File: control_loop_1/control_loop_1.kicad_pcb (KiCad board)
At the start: 2 copper layers, 100 x 95 mm, 148 parts, among them J1 I_MEAS, J10 GND, J11 -5V, J12 POW_OUT, J13 I_SET, J14 U_SET, J15 GND, J16 CTR_MODE, J17 GND, J18 CTR_MODE, J19 Limit_conn, J2 U_MEAS, J20 Trig_conn, J21 CTR_SIG, J22 CTR_SIG_OUT, J23 GND, J24 Conn_01x04, J3 GND, J4 GND, J5 +15V, J6 GND, J7 -15V, J8 SET_CONN, J9 +5V, Q1 2N7002BK, Q2 2N7002BK, Q3 2N7002BK, Q4 2N7002BK, U1 LM317EMPX/NOPB, U2 LM337IMP/NOPB, U4 OPA1679IDR, U5 OPA1679IDR, U6 DG469EQ-T1-E3, U7 OPA1679IDR, U8 LM393BIDR, U9 LM393BIDR

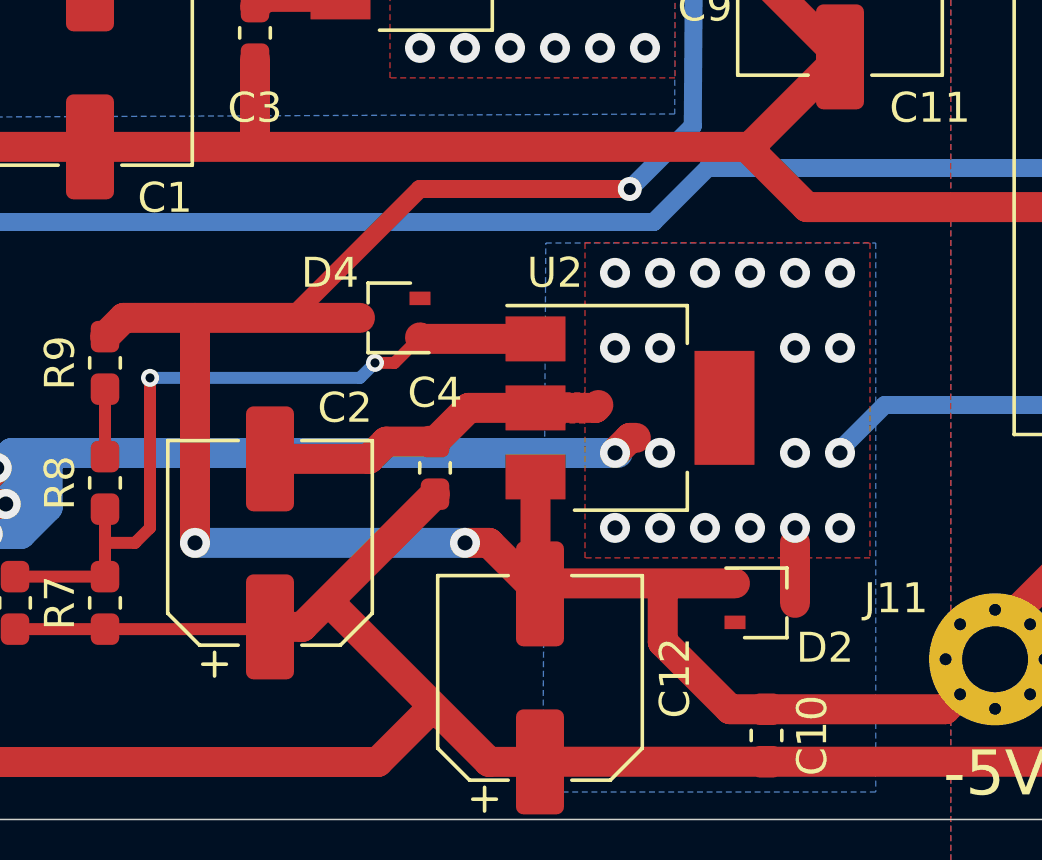
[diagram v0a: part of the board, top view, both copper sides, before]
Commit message: fixed diodes orientation
negative volt regulator - reversed diodes fixed
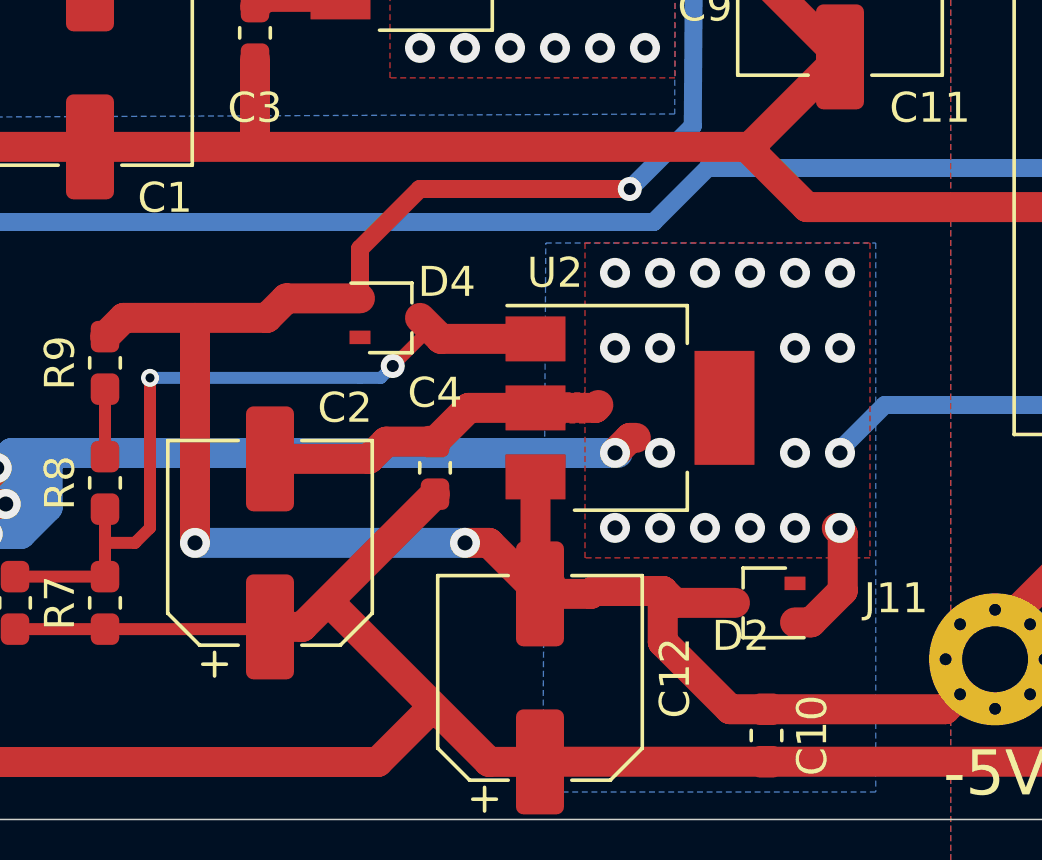
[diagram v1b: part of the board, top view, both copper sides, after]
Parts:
- turned D2 to 180 degrees
- turned D4 to 0 degrees
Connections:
- D2 pad 1: -5V -> -15V
- D2 pad 3: -15V -> -5V
- D4 pad 1: Net-(C7-Pad2) -> -5V
- D4 pad 3: -5V -> Net-(C7-Pad2)
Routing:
- net -15V: track 93.9 -> 96.1 mm
- net -5V: track 279.0 -> 278.2 mm
- net Net-(C7-Pad2): track 25.4 -> 26.2 mm
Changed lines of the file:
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@@
     (thickness 1.6)
     (drawings 70)
-    (tracks 1134)
+    (tracks 1144)
     (zones 0)
     (modules 148)
@@
   )
   (setup
-    (last_trace_width 0.25)
+    (last_trace_width 1)
     (user_trace_width 0.3)
     (user_trace_width 0.4)
@@
   )
   (module Package_TO_SOT_SMD:SOT-323_SC-70 (layer F.Cu)
-    (at 121.308 126.796 180)
+    (at 121.308 126.796)
     (descr "SOT-323, SC-70")
     (tags "SOT-323 SC-70")
     (attr smd)
-    (fp_text reference D4 (at 2 1.5) (layer F.SilkS)
+    (fp_text reference D4 (at 1.892 -1.196) (layer F.SilkS)
       (effects (font (size 1 1) (thickness 0.15)))
     )
@@
       (effects (font (size 0.5 0.5) (thickness 0.075)))
     )
-    (pad 3 smd rect (at 1 0 90) (size 0.45 0.7) (layers F.Cu F.Paste F.Mask)
-      (net 7 -5V))
-    (pad 2 smd rect (at -1 0.65 90) (size 0.45 0.7) (layers F.Cu F.Paste F.Mask)
-      (net 33 "Net-(D4-Pad2)"))
-    (pad 1 smd rect (at -1 -0.65 90) (size 0.45 0.7) (layers F.Cu F.Paste F.Mask)
+    (pad 3 smd rect (at 1 0 270) (size 0.45 0.7) (layers F.Cu F.Paste F.Mask)
       (net 5 "Net-(C7-Pad2)"))
+    (pad 2 smd rect (at -1 0.65 270) (size 0.45 0.7) (layers F.Cu F.Paste F.Mask)
+      (net 33 "Net-(D4-Pad2)"))
+    (pad 1 smd rect (at -1 -0.65 270) (size 0.45 0.7) (layers F.Cu F.Paste F.Mask)
+      (net 7 -5V))
     (model ${KISYS3DMOD}/Package_TO_SOT_SMD.3dshapes/SOT-323_SC-70.wrl
       (at (xyz 0 0 0))
@@
   )
   (module Package_TO_SOT_SMD:SOT-323_SC-70 (layer F.Cu)
-    (at 133.808 136.296)
+    (at 133.808 136.296 180)
     (descr "SOT-323, SC-70")
     (tags "SOT-323 SC-70")
     (attr smd)
-    (fp_text reference D2 (at 2 1.5) (layer F.SilkS)
+    (fp_text reference D2 (at 0.808 -1.104) (layer F.SilkS)
       (effects (font (size 1 1) (thickness 0.15)))
     )
@@
       (effects (font (size 0.5 0.5) (thickness 0.075)))
     )
-    (pad 3 smd rect (at 1 0 270) (size 0.45 0.7) (layers F.Cu F.Paste F.Mask)
-      (net 3 -15V))
-    (pad 2 smd rect (at -1 0.65 270) (size 0.45 0.7) (layers F.Cu F.Paste F.Mask)
-      (net 31 "Net-(D2-Pad2)"))
-    (pad 1 smd rect (at -1 -0.65 270) (size 0.45 0.7) (layers F.Cu F.Paste F.Mask)
+    (pad 3 smd rect (at 1 0 90) (size 0.45 0.7) (layers F.Cu F.Paste F.Mask)
       (net 7 -5V))
+    (pad 2 smd rect (at -1 0.65 90) (size 0.45 0.7) (layers F.Cu F.Paste F.Mask)
+      (net 31 "Net-(D2-Pad2)"))
+    (pad 1 smd rect (at -1 -0.65 90) (size 0.45 0.7) (layers F.Cu F.Paste F.Mask)
+      (net 3 -15V))
     (model ${KISYS3DMOD}/Package_TO_SOT_SMD.3dshapes/SOT-323_SC-70.wrl
       (at (xyz 0 0 0))
@@
   (segment (start 123.933 129.796) (end 126.158 129.796) (width 1) (layer F.Cu) (net 3))
   (segment (start 122.808 130.921) (end 123.933 129.796) (width 1) (layer F.Cu) (net 3))
-  (segment (start 134.808 136.296) (end 134.808 135.071) (width 1) (layer F.Cu) (net 3))
-  (segment (start 134.808 135.071) (end 134.808 134.296) (width 1) (layer F.Cu) (net 3))
   (segment (start 129.307999 130.796001) (end 129.503999 130.796001) (width 1) (layer F.Cu) (net 3))
   (segment (start 128.808 131.296) (end 129.307999 130.796001) (width 1) (layer F.Cu) (net 3))
@@
   (segment (start 159.836 129.7) (end 137.8 129.7) (width 0.6) (layer B.Cu) (net 3))
   (segment (start 137.8 129.7) (end 136.3 131.2) (width 0.6) (layer B.Cu) (net 3))
+  (segment (start 135.343002 136.946) (end 136.4 135.889002) (width 1) (layer F.Cu) (net 3))
+  (segment (start 134.808 136.946) (end 135.343002 136.946) (width 1) (layer F.Cu) (net 3))
+  (segment (start 136.4 135.889002) (end 136.4 134) (width 1) (layer F.Cu) (net 3))
+  (segment (start 136.4 134) (end 136.2 133.8) (width 1) (layer F.Cu) (net 3))
   (segment (start 130.458 107.646) (end 130.108 107.296) (width 1) (layer F.Cu) (net 4))
   (segment (start 131.808 107.646) (end 130.458 107.646) (width 1) (layer F.Cu) (net 4))
@@
   (segment (start 119.308 108.796) (end 119.808 108.796) (width 0.4) (layer F.Cu) (net 4))
   (segment (start 116.683 102.796) (end 116.683 105.796) (width 0.4) (layer F.Cu) (net 4))
-  (segment (start 122.358 127.496) (end 122.308 127.446) (width 1) (layer F.Cu) (net 5))
-  (segment (start 126.158 127.496) (end 122.358 127.496) (width 1) (layer F.Cu) (net 5))
   (segment (start 108.808 135.421) (end 111.808 135.421) (width 0.4) (layer F.Cu) (net 5))
   (segment (start 111.808 133.171) (end 111.808 134.296) (width 0.4) (layer F.Cu) (net 5))
-  (segment (start 111.808 134.296) (end 112.808 134.296) (width 0.4) (layer F.Cu) (net 5))
   (segment (start 111.808 134.296) (end 111.808 135.421) (width 0.4) (layer F.Cu) (net 5))
-  (segment (start 112.808 134.296) (end 113.308 133.796) (width 0.4) (layer F.Cu) (net 5))
   (via (at 113.308 128.796) (size 0.6) (drill 0.3) (layers F.Cu B.Cu) (net 5))
+  (segment (start 111.808 134.296) (end 112.808 134.296) (width 0.4) (layer F.Cu) (net 5))
   (segment (start 113.308 133.796) (end 113.308 128.796) (width 0.4) (layer F.Cu) (net 5))
+  (segment (start 112.808 134.296) (end 113.308 133.796) (width 0.4) (layer F.Cu) (net 5))
   (segment (start 113.308 128.796) (end 120.308 128.796) (width 0.4) (layer B.Cu) (net 5))
-  (via (at 120.808 128.296) (size 0.6) (drill 0.3) (layers F.Cu B.Cu) (net 5))
-  (segment (start 120.308 128.796) (end 120.808 128.296) (width 0.4) (layer B.Cu) (net 5))
-  (segment (start 121.458 128.296) (end 122.308 127.446) (width 0.4) (layer F.Cu) (net 5))
-  (segment (start 120.808 128.296) (end 121.458 128.296) (width 0.4) (layer F.Cu) (net 5))
+  (segment (start 123.008 127.496) (end 122.308 126.796) (width 1) (layer F.Cu) (net 5))
+  (segment (start 126.158 127.496) (end 123.008 127.496) (width 1) (layer F.Cu) (net 5))
+  (segment (start 120.308 128.796) (end 121.004 128.796) (width 0.4) (layer B.Cu) (net 5))
+  (via (at 121.4 128.4) (size 0.8) (drill 0.4) (layers F.Cu B.Cu) (net 5))
+  (segment (start 121.004 128.796) (end 121.4 128.4) (width 0.4) (layer B.Cu) (net 5))
+  (segment (start 121.4 128.4) (end 122.4 127.4) (width 0.4) (layer F.Cu) (net 5))
+  (segment (start 122.4 127.4) (end 122.8 127.4) (width 0.4) (layer F.Cu) (net 5))
   (via (at 122.308 117.796) (size 1) (drill 0.5) (layers F.Cu B.Cu) (net 6))
   (via (at 122.308 115.296) (size 1) (drill 0.5) (layers F.Cu B.Cu) (net 6))
@@
   (segment (start 126.158 132.096) (end 126.158 135.846) (width 1) (layer F.Cu) (net 7))
   (segment (start 126.658 135.646) (end 126.308 135.996) (width 1) (layer F.Cu) (net 7))
-  (segment (start 132.808 135.646) (end 126.658 135.646) (width 1) (layer F.Cu) (net 7))
   (segment (start 112.433 126.796) (end 111.808 127.421) (width 1) (layer F.Cu) (net 7))
   (segment (start 114.808 126.796) (end 114.808 134.296) (width 1) (layer F.Cu) (net 7))
-  (segment (start 120.308 126.796) (end 114.808 126.796) (width 1) (layer F.Cu) (net 7))
   (segment (start 114.808 126.796) (end 112.433 126.796) (width 1) (layer F.Cu) (net 7))
   (via (at 114.808 134.296) (size 1) (drill 0.5) (layers F.Cu B.Cu) (net 7))
@@
   (via (at 129.3 122.5) (size 0.8) (drill 0.4) (layers F.Cu B.Cu) (net 7))
   (segment (start 129.3 122.5) (end 122.3 122.5) (width 0.6) (layer F.Cu) (net 7))
-  (segment (start 122.3 122.5) (end 118 126.8) (width 0.6) (layer F.Cu) (net 7))
   (segment (start 158.463 68.766) (end 157.334 68.766) (width 0.4) (layer F.Cu) (net 7))
   (segment (start 156.863 69.237) (end 156.863 74.266) (width 0.4) (layer F.Cu) (net 7))
@@
   (segment (start 127.699999 101.099999) (end 131.5 104.9) (width 0.6) (layer B.Cu) (net 7))
   (segment (start 131.5 104.9) (end 131.5 106) (width 0.6) (layer B.Cu) (net 7))
+  (segment (start 114.808 126.796) (end 117.204 126.796) (width 1) (layer F.Cu) (net 7))
+  (segment (start 117.854 126.146) (end 120.308 126.146) (width 1) (layer F.Cu) (net 7))
+  (segment (start 117.204 126.796) (end 117.854 126.146) (width 1) (layer F.Cu) (net 7))
+  (segment (start 120.308 124.492) (end 120.308 126.146) (width 0.6) (layer F.Cu) (net 7))
+  (segment (start 122.3 122.5) (end 120.308 124.492) (width 0.6) (layer F.Cu) (net 7))
+  (segment (start 130.4 135.9) (end 128.1 135.9) (width 1) (layer F.Cu) (net 7))
+  (segment (start 128.004 135.996) (end 126.308 135.996) (width 1) (layer F.Cu) (net 7))
+  (segment (start 128.1 135.9) (end 128.004 135.996) (width 1) (layer F.Cu) (net 7))
+  (segment (start 130.796 136.296) (end 132.808 136.296) (width 1) (layer F.Cu) (net 7))
+  (segment (start 130.4 135.9) (end 130.796 136.296) (width 1) (layer F.Cu) (net 7))
   (segment (start 120.613 75.016) (end 120.613 73.266) (width 0.3) (layer F.Cu) (net 8))
   (segment (start 123.513 71.286) (end 121.414 71.286) (width 0.3) (layer F.Cu) (net 8))
